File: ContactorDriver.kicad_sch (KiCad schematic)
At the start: 41 parts, among them J1 PowerConn, J2 DashboardConn, J3 DashboardConn, J4 ContactorConn, J5 PrechargeConn, J6 PrechargeResistorConn, J7 PrechargeResistor, J8 PrechargeResistor, Q1 NTR4003NT1G, Q2 NTR4003NT1G, Q3 CSD18511KTT, Q4 CSD18511KTT, SW1 SW_Push, SW2 SW_Push, SW3 SW_Push

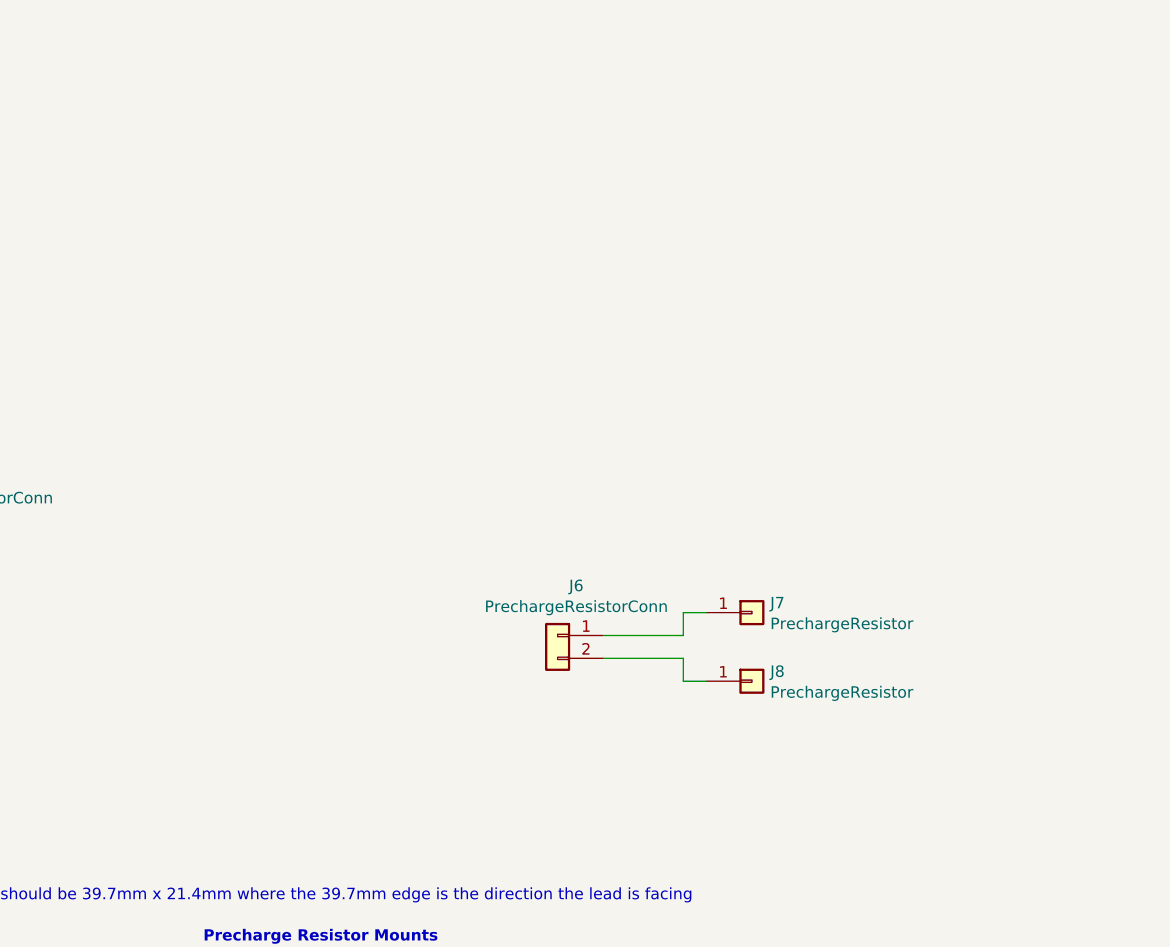
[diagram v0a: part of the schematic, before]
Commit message: Contactor driver pcb standardization (#2)
* Added pull request document to repository

* added backup files to .gitignore

* modified .gitignore for backups, made a typo on previous commit

* Adds pdfs of layout and schematic with version histories included in the files

* adds files for schematic and layout that include version history and dimensions

* Adds submodule correctly I believe

* adds BOM to repository

* adds last version of README I can complete at this time

* updates BOM to include horizontal connectors instead of vertical ones

* Fixed error in footprint

* Adds 3D models to the layout and deletes an empty folder

* Adds board function as far as I know, and includes the pdf change as well

* This should finally hav the correct 3D models, although I'm unsure why they weren't there already

* Wanted to ensure last save was included

* Formats version history better, adds datasheets for all components on schematic, and puts board dimension on user comments layer
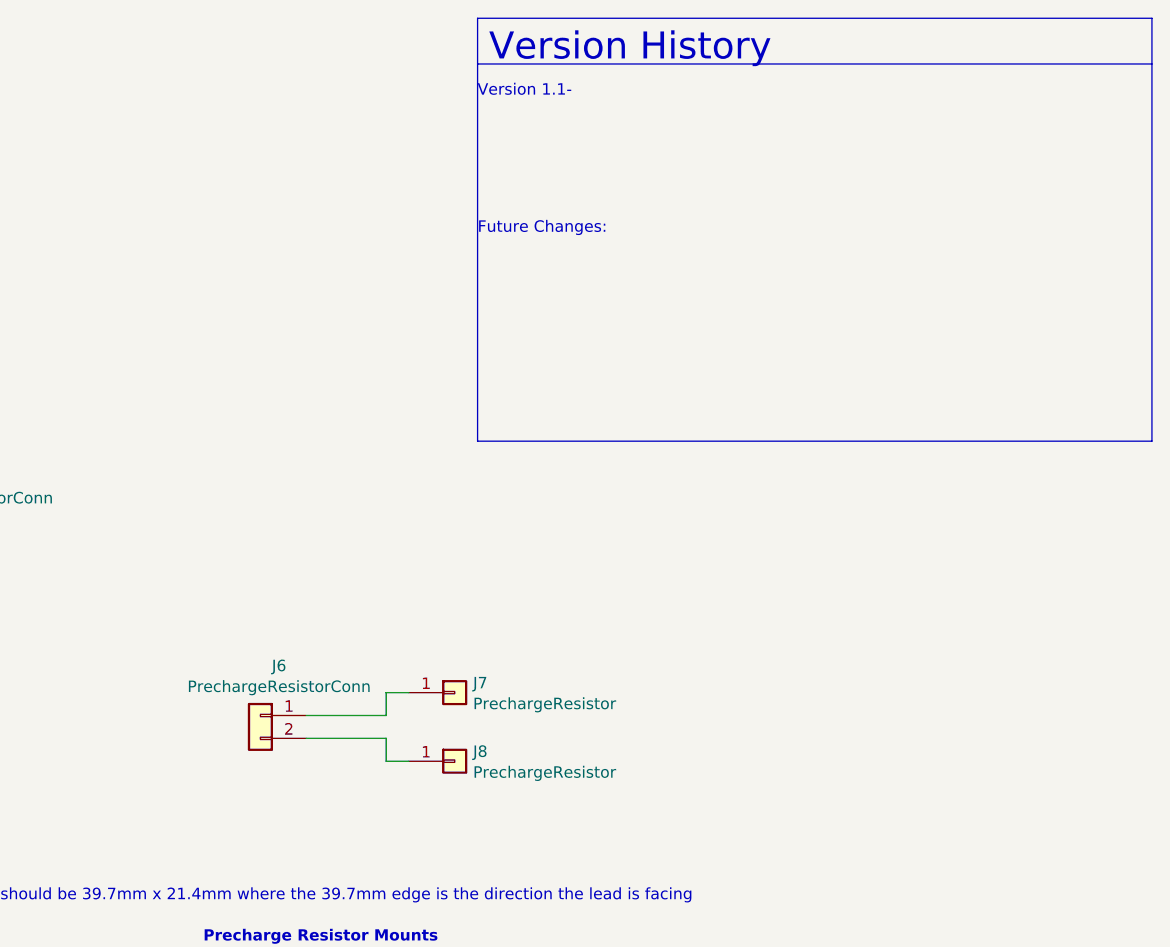
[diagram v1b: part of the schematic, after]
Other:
- note added: "Future Changes:"
- note added: "Version 1.1-"
- note added: "Version History"
- moved on the sheet: J6, J7, J8

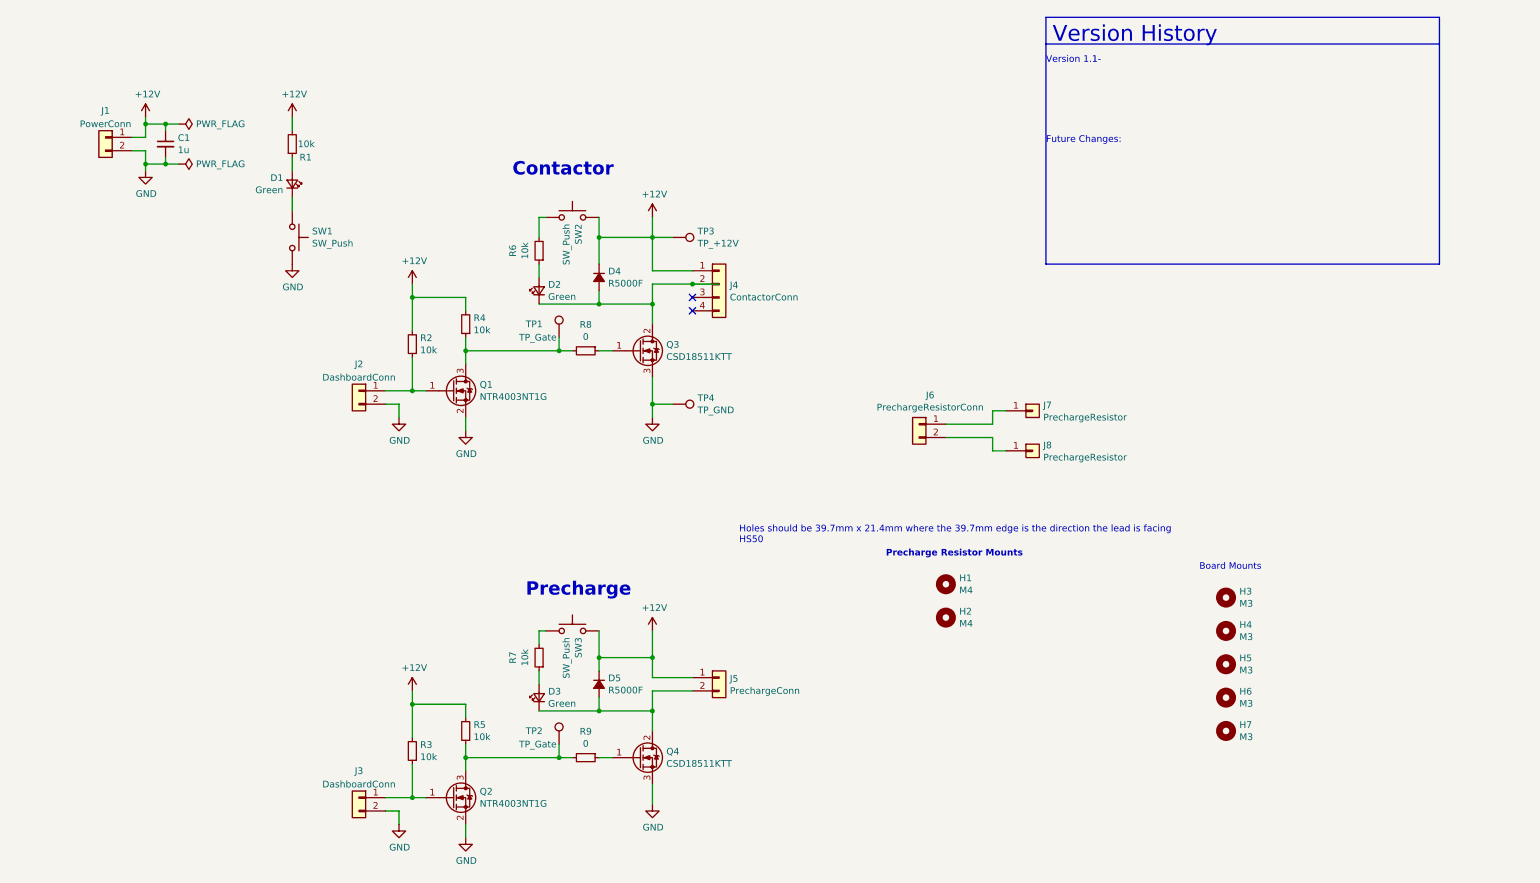
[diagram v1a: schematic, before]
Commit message: Updated Contactor Driver Schematic
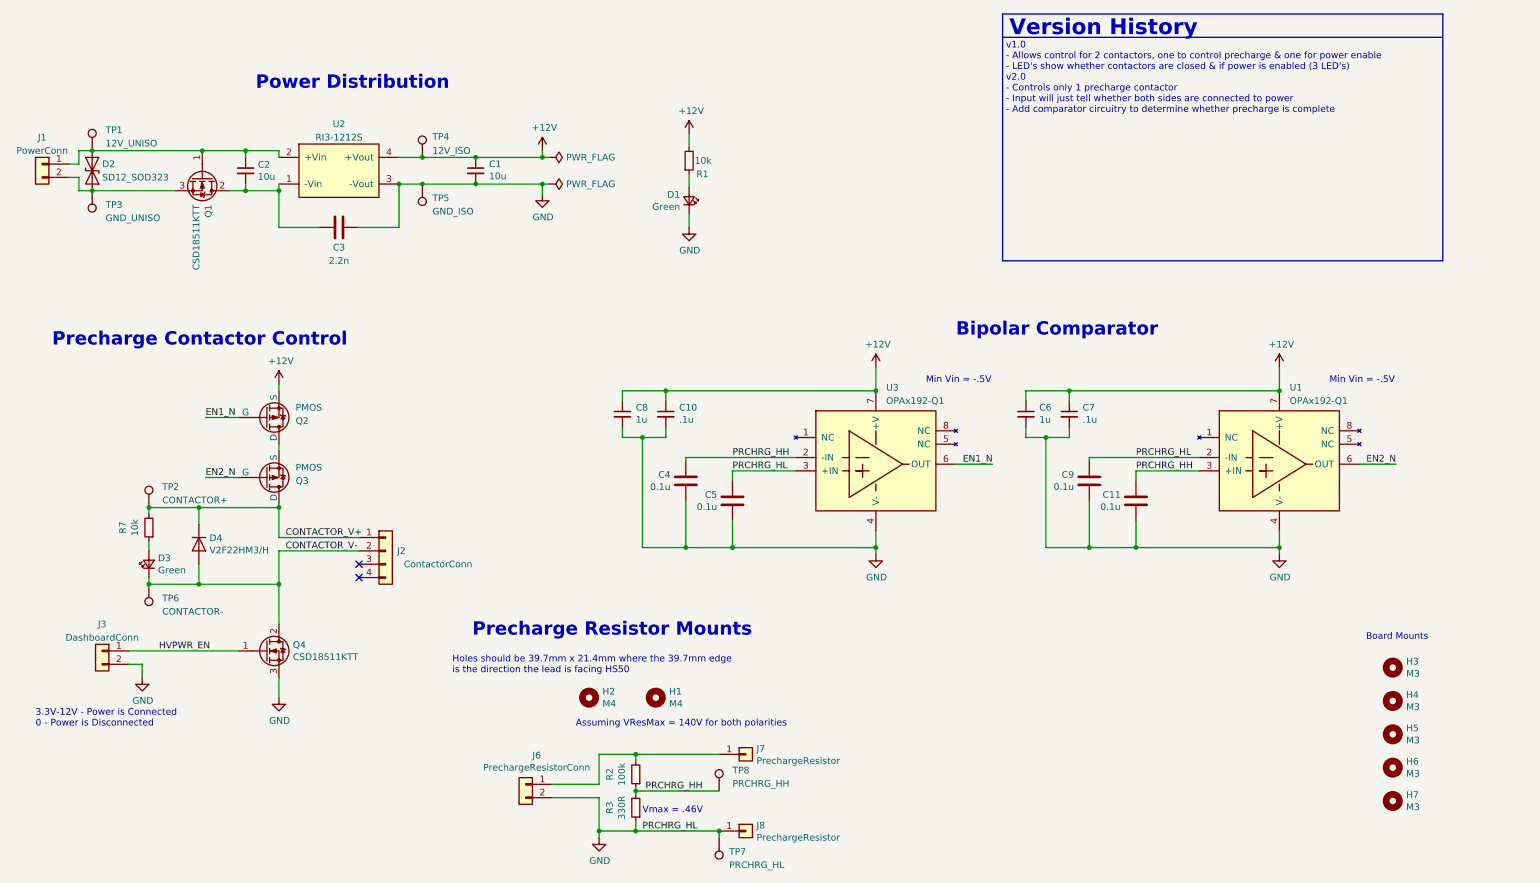
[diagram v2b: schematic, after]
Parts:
- removed D2: Green, LED_SMD:LED_0805_2012Metric_Pad1.15x1.40mm_HandSolder, symbol Device:LED_Small
- removed D4, D5: R5000F, UTSVT_Passive:V2F22HM, symbol ContactorDriver-rescue:D_Small_ALT-Device
- removed J2: DashboardConn, Connector_Molex:Molex_Micro-Fit_3.0_43650-0215_1x02_P3.00mm_Vertical, symbol Connector_Generic:Conn_01x02
- removed J4: ContactorConn, Connector_Molex:Molex_Micro-Fit_3.0_43650-0415_1x04_P3.00mm_Vertical, symbol Connector_Generic:Conn_01x04
- removed J5: PrechargeConn, Connector_Molex:Molex_Micro-Fit_3.0_43650-0215_1x02_P3.00mm_Vertical, symbol Connector_Generic:Conn_01x02
- removed Q1, Q2: NTR4003NT1G, Package_TO_SOT_SMD:TSOT-23, symbol Device:Q_NMOS_GSD
- removed Q3: CSD18511KTT, Package_TO_SOT_SMD:TO-252-2, symbol Device:Q_NMOS_GDS
- removed R4, R5, R6: 10k, Resistor_SMD:R_0805_2012Metric_Pad1.15x1.40mm_HandSolder, symbol Device:R_Small
- removed R8, R9: 0, Resistor_SMD:R_0805_2012Metric_Pad1.15x1.40mm_HandSolder, symbol Device:R_Small
- removed SW1, SW2, SW3: SW_Push, Button_Switch_SMD:SW_SPST_B3SL-1002P, symbol Switch:SW_Push
- added C10, C7: .1u, Capacitor_SMD:C_0805_2012Metric_Pad1.15x1.40mm_HandSolder, symbol Device:C_Small
- added C11, C4, C5, C9: 0.1u, Capacitor_SMD:C_0805_2012Metric, symbol Device:C
- added C2: 10u, Capacitor_SMD:C_0805_2012Metric_Pad1.15x1.40mm_HandSolder, symbol Device:C_Small
- added C3: 2.2n, Capacitor_SMD:C_0805_2012Metric, symbol Device:C
- added C6, C8: 1u, Capacitor_SMD:C_0805_2012Metric_Pad1.15x1.40mm_HandSolder, symbol Device:C_Small
- added D2: SD12_SOD323, Diode_SMD:D_SOD-323, symbol Diode:SD12_SOD323
- added D4: V2F22HM3/H, UTSVT_Passive:V2F22HM, symbol Device:D
- added J2: ContactorConn, UTSVT_Connectors:Molex_MicroFit3.0_1x4xP3.00mm_PolarizingPeg_Vertical, symbol Connector_Generic:Conn_01x04
- added Q1: CSD18511KTT, Package_TO_SOT_SMD:TO-252-2, symbol Device:Q_NMOS_GDS
- added Q2, Q3: PMOS, Package_TO_SOT_THT:TO-220-3_Vertical, symbol Simulation_SPICE:PMOS
- added TP5: GND_ISO, TestPoint:TestPoint_Keystone_5005-5009_Compact, symbol Connector:TestPoint
- added TP6: CONTACTOR-, TestPoint:TestPoint_Keystone_5005-5009_Compact, symbol Connector:TestPoint
- added TP7: PRCHRG_HL, TestPoint:TestPoint_Keystone_5005-5009_Compact, symbol Connector:TestPoint
- added TP8: PRCHRG_HH, TestPoint:TestPoint_Keystone_5005-5009_Compact, symbol Connector:TestPoint
- added U1, U3: OPAx192-Q1, Package_SO:VSSOP-8_3.0x3.0mm_P0.65mm, symbol utsvt-chips:OPAx192-Q1
- added U2: RI3-1212S, UTSVT_ICs:RI3_DC_Converter, symbol utsvt-power-regulators:RI3-xxxxS
- C1: value 1u -> 10u
- R2: value 10k -> 100k
- R3: value 10k -> 330R
- TP1: value TP_Gate -> 12V_UNISO
- TP2: value TP_Gate -> CONTACTOR+
- TP3: value TP_+12V -> GND_UNISO
- TP4: value TP_GND -> 12V_ISO
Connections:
- net +12V: now also TP4.1, C10.1, C6.1, C7.1, C8.1, Q2.3 (S), U1.7 (+V), U2.4 (+Vout), U3.7 (+V); no longer J1.1 (Pin_1), R2.2, R3.2, TP3.1
- net GND: now also D1.1 (K), J6.2 (Pin_2), J8.1 (Pin_1), R3.1, C10.2, C11.2, C3.2, C4.2, C5.1, C5.2, C6.2, C7.2, C8.2, C9.1, C9.2, TP5.1, TP7.1, U1.2 (-IN), U1.4 (V-), U2.3 (-Vout), U3.3 (+IN), U3.4 (V-); no longer J1.2 (Pin_2), TP4.1
- net PRCHRG_HH: now reaches R2.1
- net PRCHRG_HH: now also R3.2, C11.1, C4.1, TP8.1, U1.3 (+IN), U3.2 (-IN)
- net at TP1.1: now also J1.1 (Pin_1), C2.1, D2.2 (A2), Q1.1 (G), U2.2 (+Vin)
- net HVPWR_EN: now reaches J3.1 (Pin_1)
- net HVPWR_EN: now also Q4.1 (G); no longer R3.1
- net CONTACTOR_V+: now reaches TP2.1
- net CONTACTOR_V+: now also R7.2, D4.1 (K), J2.1 (Pin_1), Q3.1 (D)
- net CONTACTOR_V-: now reaches D3.1 (K), Q4.2 (D)
- net CONTACTOR_V-: now also D4.2 (A), J2.2 (Pin_2), TP6.1
- net at J6.1 (Pin_1), J7.1 (Pin_1): now also R2.2
- new net: D2.1 (A1), J1.2 (Pin_2), Q1.3 (S), TP3.1
- new net: C2.2, C3.1, Q1.2 (D), U2.1 (-Vin)
- new net: Q2.1 (D), Q3.3 (S)
- new net EN1_N: Q2.2 (G), U3.6 (OUT)
- new net EN2_N: Q3.2 (G), U1.6 (OUT)
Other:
- note added: "3.3V-12V - Power is Connected 0 - Power is Disconnected"
- note added: "Assuming VResMax = 140V for both polarities"
- note added: "Bipolar Comparator"
- note added: "Min Vin = -.5V"
- note added: "Power Distribution"
- note added: "Precharge Contactor Control"
- note added: "Vmax = .46V"
- note added: "v1.0 - Allows control for 2 contactors, one to control precharge & one for power enable - LED's show whether contactors are closed & if power is enabled (3 LED's) v2.0 - Controls only 1 precharge contactor - Input will just tell whether both sides are connected to power - Add comparator circuitry to determine whether precharge is complete"
- note removed: "Contactor"
- note removed: "Future Changes:"
- note removed: "Precharge"
- note removed: "Version 1.1-"
- moved on the sheet: C1, D1, D3, H1, H2, H3, H4, H5, H6, H7, J1, J3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

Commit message: Added ferrite beads
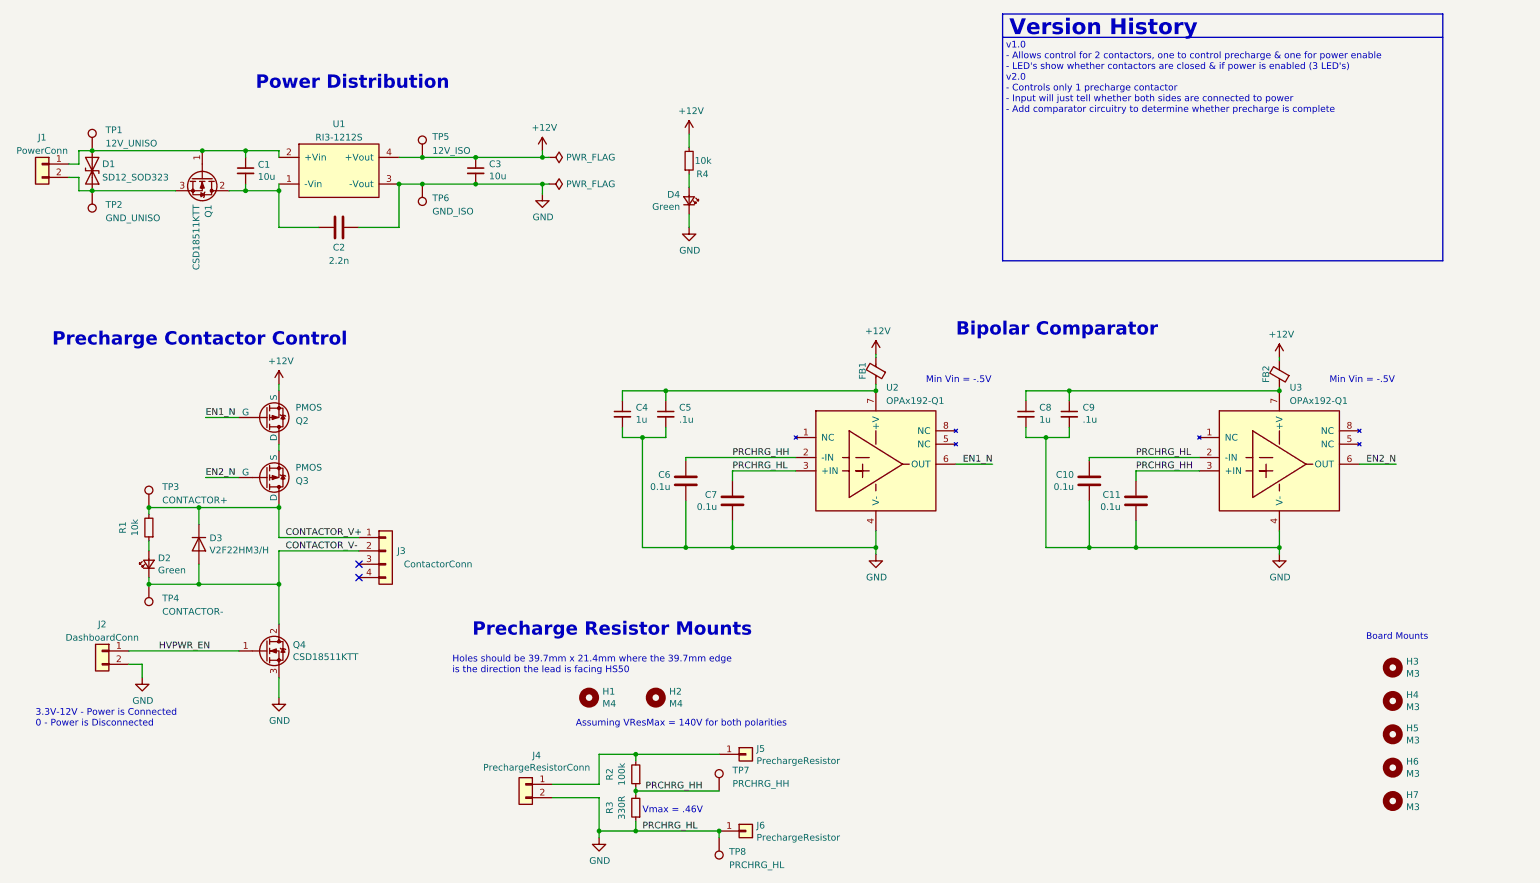
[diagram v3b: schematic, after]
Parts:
- added FB1, FB2: FerriteBead_Small, Inductor_SMD:L_0805_2012Metric, symbol Device:FerriteBead_Small
- C1: renamed from C2; footprint Capacitor_SMD:C_0805_2012Metric_Pad1.15x1.40mm_HandSolder -> Capacitor_SMD:C_0805_2012Metric
- C3: renamed from C1; footprint Capacitor_SMD:C_0805_2012Metric_Pad1.15x1.40mm_HandSolder -> Capacitor_SMD:C_0805_2012Metric
- C4: renamed from C8; footprint Capacitor_SMD:C_0805_2012Metric_Pad1.15x1.40mm_HandSolder -> Capacitor_SMD:C_0805_2012Metric
- C5: renamed from C10; footprint Capacitor_SMD:C_0805_2012Metric_Pad1.15x1.40mm_HandSolder -> Capacitor_SMD:C_0805_2012Metric
- C8: renamed from C6; footprint Capacitor_SMD:C_0805_2012Metric_Pad1.15x1.40mm_HandSolder -> Capacitor_SMD:C_0805_2012Metric
- C9: renamed from C7; footprint Capacitor_SMD:C_0805_2012Metric_Pad1.15x1.40mm_HandSolder -> Capacitor_SMD:C_0805_2012Metric
- R1: renamed from R7; footprint Resistor_SMD:R_0805_2012Metric_Pad1.15x1.40mm_HandSolder -> Resistor_SMD:R_0805_2012Metric
- R2, R3: footprint Resistor_SMD:R_0805_2012Metric_Pad1.15x1.40mm_HandSolder -> Resistor_SMD:R_0805_2012Metric
- R4: renamed from R1; footprint Resistor_SMD:R_0805_2012Metric_Pad1.15x1.40mm_HandSolder -> Resistor_SMD:R_0805_2012Metric
- renumbered C9 to C10, C3 to C2, C4 to C6, C5 to C7, D2 to D1, D3 to D2, D4 to D3, D1 to D4, H2 to H1, H1 to H2, J3 to J2, J2 to J3, J6 to J4, J7 to J5, J8 to J6, TP3 to TP2, TP2 to TP3, TP6 to TP4, TP4 to TP5, TP5 to TP6, TP8 to TP7, TP7 to TP8, U2 to U1, U3 to U2, U1 to U3
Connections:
- net +12V: now also FB1.2, FB2.2; no longer C4.1, C5.1, C8.1, C9.1, U2.7 (+V), U3.7 (+V)
- new net: C4.1, C5.1, FB1.1, U2.7 (+V)
- new net: C8.1, C9.1, FB2.1, U3.7 (+V)
